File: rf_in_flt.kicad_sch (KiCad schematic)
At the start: 1 part, among them J2 N_PAD

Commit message: WIP rev C
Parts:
- renumbered J2 to J7
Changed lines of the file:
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@@
   (title_block
     (title "Remote Radio Unit - RF board")
-    (date "20-01-2024")
-    (rev "B")
+    (date "04-04-2024")
+    (rev "C")
     (company "M17 Project")
     (comment 1 "Wojciech Kaczmarski, SP5WWP")
@@
   (symbol (lib_id "Connector:Conn_Coaxial") (at 215.9 138.43 0) (unit 1)
     (in_bom yes) (on_board yes) (dnp no) (fields_autoplaced)
-    (property "Reference" "J2" (at 218.4401 137.5111 0)
+    (property "Reference" "J7" (at 218.4401 137.5111 0)
       (effects (font (size 1.27 1.27)) (justify left))
     )
@@
     (instances
       (project "m17-rru-rf"
-        (path "/4c42207c-9e6b-42da-ad38-da126b892014/59b2721c-5b8a-4fc3-bf5e-590dec787afb"
-          (reference "J2") (unit 1)
-        )
         (path "/4c42207c-9e6b-42da-ad38-da126b892014/548d001d-7c84-4d2c-957b-c97be3023400"
           (reference "J7") (unit 1)
@@
   (symbol (lib_id "power:GND") (at 215.9 144.78 0) (unit 1)
     (in_bom yes) (on_board yes) (dnp no) (fields_autoplaced)
-    (property "Reference" "#PWR051" (at 215.9 151.13 0)
+    (property "Reference" "#PWR0139" (at 215.9 151.13 0)
       (effects (font (size 1.27 1.27)) hide)
     )
@@
     (instances
       (project "m17-rru-rf"
-        (path "/4c42207c-9e6b-42da-ad38-da126b892014/59b2721c-5b8a-4fc3-bf5e-590dec787afb"
-          (reference "#PWR051") (unit 1)
-        )
         (path "/4c42207c-9e6b-42da-ad38-da126b892014/548d001d-7c84-4d2c-957b-c97be3023400"
-          (reference "#PWR0129") (unit 1)
+          (reference "#PWR0139") (unit 1)
         )
       )

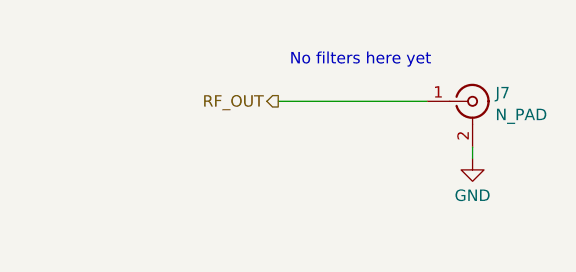
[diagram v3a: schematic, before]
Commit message: Rev C
- lowpass at RF in
- lowpass after RF PA
- pulldown at TP2 (BOOT1)
- CC1200 clocking fixed
- PCB render/PDF update
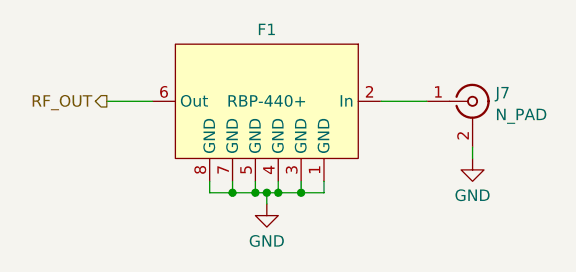
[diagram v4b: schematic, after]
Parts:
- added F1: RBP-440+, Parts:RBP_CASE, symbol Parts:RBP-440+
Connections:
- net GND: now also F1.1 (GND), F1.3 (GND), F1.4 (GND), F1.5 (GND), F1.7 (GND), F1.8 (GND)
- net RF_OUT: now also F1.6 (Out); no longer J7.1 (In)
- new net: F1.2 (In), J7.1 (In)
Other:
- note removed: "No filters here yet"
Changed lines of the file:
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@@
     (comment 1 "Wojciech Kaczmarski, SP5WWP")
   )
-  (wire (pts (xy 194.31 138.43) (xy 210.82 138.43))
+  (junction (at 194.31 148.59) (diameter 0) (color 0 0 0 0)
+  )
+  (junction (at 191.77 148.59) (diameter 0) (color 0 0 0 0)
+  )
+  (junction (at 196.85 148.59) (diameter 0) (color 0 0 0 0)
+  )
+  (junction (at 189.23 148.59) (diameter 0) (color 0 0 0 0)
+  )
+  (junction (at 193.04 148.59) (diameter 0) (color 0 0 0 0)
+  )
+  (wire (pts (xy 196.85 147.32) (xy 196.85 148.59))
+    (stroke (width 0) (type default))
+  )
+  (wire (pts (xy 189.23 148.59) (xy 191.77 148.59))
+    (stroke (width 0) (type default))
+  )
+  (wire (pts (xy 199.39 147.32) (xy 199.39 148.59))
+    (stroke (width 0) (type default))
+  )
+  (wire (pts (xy 189.23 147.32) (xy 189.23 148.59))
+    (stroke (width 0) (type default))
+  )
+  (wire (pts (xy 191.77 147.32) (xy 191.77 148.59))
+    (stroke (width 0) (type default))
+  )
+  (wire (pts (xy 194.31 147.32) (xy 194.31 148.59))
+    (stroke (width 0) (type default))
+  )
+  (wire (pts (xy 186.69 148.59) (xy 189.23 148.59))
+    (stroke (width 0) (type default))
+  )
+  (wire (pts (xy 175.26 138.43) (xy 180.34 138.43))
+    (stroke (width 0) (type default))
+  )
+  (wire (pts (xy 191.77 148.59) (xy 193.04 148.59))
+    (stroke (width 0) (type default))
+  )
+  (wire (pts (xy 194.31 148.59) (xy 193.04 148.59))
+    (stroke (width 0) (type default))
+  )
+  (wire (pts (xy 196.85 148.59) (xy 199.39 148.59))
     (stroke (width 0) (type default))
   )
@@
     (stroke (width 0) (type default))
   )
-  (text "No filters here yet" (at 195.58 134.62 0)
-    (effects (font (size 1.27 1.27)) (justify left bottom))
+  (wire (pts (xy 193.04 148.59) (xy 193.04 149.86))
+    (stroke (width 0) (type default))
   )
-  (hierarchical_label "RF_OUT" (shape output) (at 194.31 138.43 180) (fields_autoplaced)
+  (wire (pts (xy 196.85 148.59) (xy 194.31 148.59))
+    (stroke (width 0) (type default))
+  )
+  (wire (pts (xy 205.74 138.43) (xy 210.82 138.43))
+    (stroke (width 0) (type default))
+  )
+  (wire (pts (xy 186.69 147.32) (xy 186.69 148.59))
+    (stroke (width 0) (type default))
+  )
+  (hierarchical_label "RF_OUT" (shape output) (at 175.26 138.43 180) (fields_autoplaced)
     (effects (font (size 1.27 1.27)) (justify right))
   )
@@
     )
   )
+  (symbol (lib_id "Parts:RBP-440+") (at 193.04 138.43 0) (mirror y) (unit 1)
+    (in_bom yes) (on_board yes) (dnp no)
+    (property "Reference" "F1" (at 193.04 130.4869 0)
+      (effects (font (size 1.27 1.27)))
+    )
+    (property "Value" "RBP-440+" (at 193.04 138.43 0)
+      (effects (font (size 1.27 1.27)))
+    )
+    (property "Footprint" "Parts:RBP_CASE" (at 193.04 138.43 0)
+      (effects (font (size 1.27 1.27)) hide)
+    )
+    (property "Datasheet" "" (at 193.04 138.43 0)
+      (effects (font (size 1.27 1.27)) hide)
+    )
+    (property "PN" "RBP-440+" (at 193.04 138.43 0)
+      (effects (font (size 1.27 1.27)) hide)
+    )
+    (property "MPN" "RBP-440+" (at 193.04 138.43 0)
+      (effects (font (size 1.27 1.27)) hide)
+    )
+    (pin "7")
+    (pin "6")
+    (pin "5")
+    (pin "8")
+    (pin "1")
+    (pin "2")
+    (pin "4")
+    (pin "3")
+    (instances
+      (project "m17-rru-rf"
+        (path "/4c42207c-9e6b-42da-ad38-da126b892014/548d001d-7c84-4d2c-957b-c97be3023400"
+          (reference "F1") (unit 1)
+        )
+      )
+    )
+  )
+  (symbol (lib_id "power:GND") (at 193.04 149.86 0) (unit 1)
+    (in_bom yes) (on_board yes) (dnp no) (fields_autoplaced)
+    (property "Reference" "#PWR0139" (at 193.04 156.21 0)
+      (effects (font (size 1.27 1.27)) hide)
+    )
+    (property "Value" "GND" (at 193.04 153.9931 0)
+      (effects (font (size 1.27 1.27)))
+    )
+    (property "Footprint" "" (at 193.04 149.86 0)
+      (effects (font (size 1.27 1.27)) hide)
+    )
+    (property "Datasheet" "" (at 193.04 149.86 0)
+      (effects (font (size 1.27 1.27)) hide)
+    )
+    (pin "1")
+    (instances
+      (project "m17-rru-rf"
+        (path "/4c42207c-9e6b-42da-ad38-da126b892014/548d001d-7c84-4d2c-957b-c97be3023400"
+          (reference "#PWR0139") (unit 1)
+        )
+      )
+    )
+  )
   (symbol (lib_id "power:GND") (at 215.9 144.78 0) (unit 1)
     (in_bom yes) (on_board yes) (dnp no) (fields_autoplaced)
-    (property "Reference" "#PWR0139" (at 215.9 151.13 0)
+    (property "Reference" "#PWR0140" (at 215.9 151.13 0)
       (effects (font (size 1.27 1.27)) hide)
     )
@@
       (project "m17-rru-rf"
         (path "/4c42207c-9e6b-42da-ad38-da126b892014/548d001d-7c84-4d2c-957b-c97be3023400"
-          (reference "#PWR0139") (unit 1)
+          (reference "#PWR0140") (unit 1)
         )
       )
